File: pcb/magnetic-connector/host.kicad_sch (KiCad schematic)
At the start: 8 parts

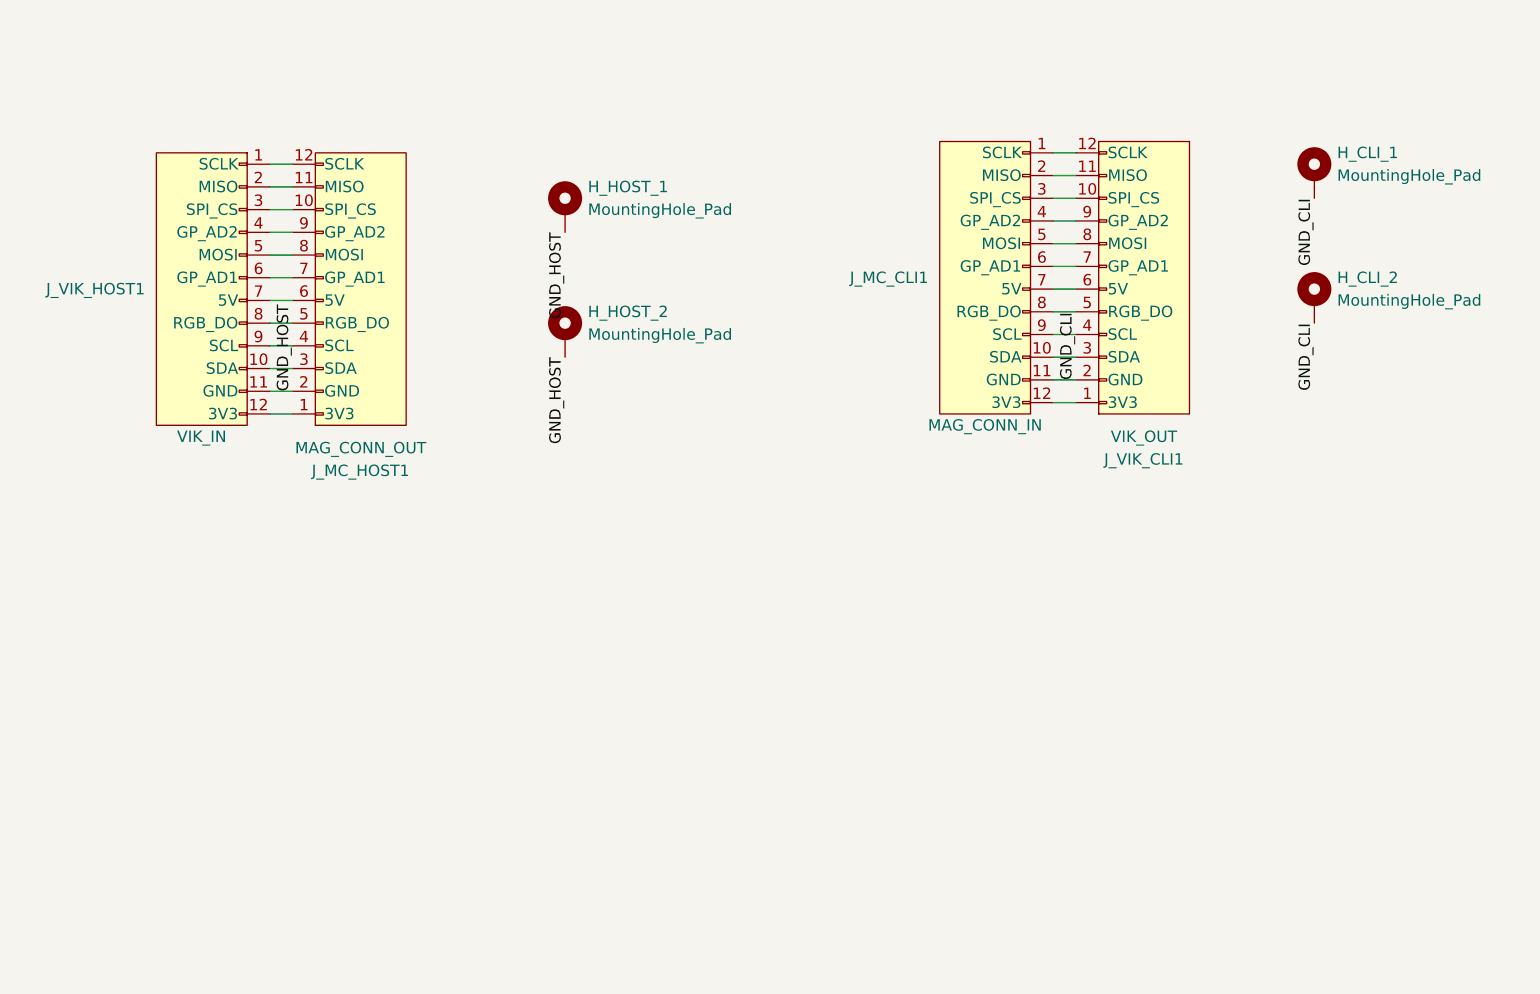
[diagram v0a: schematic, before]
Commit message: Make magnetic connector size compliant with VIK small form factor.
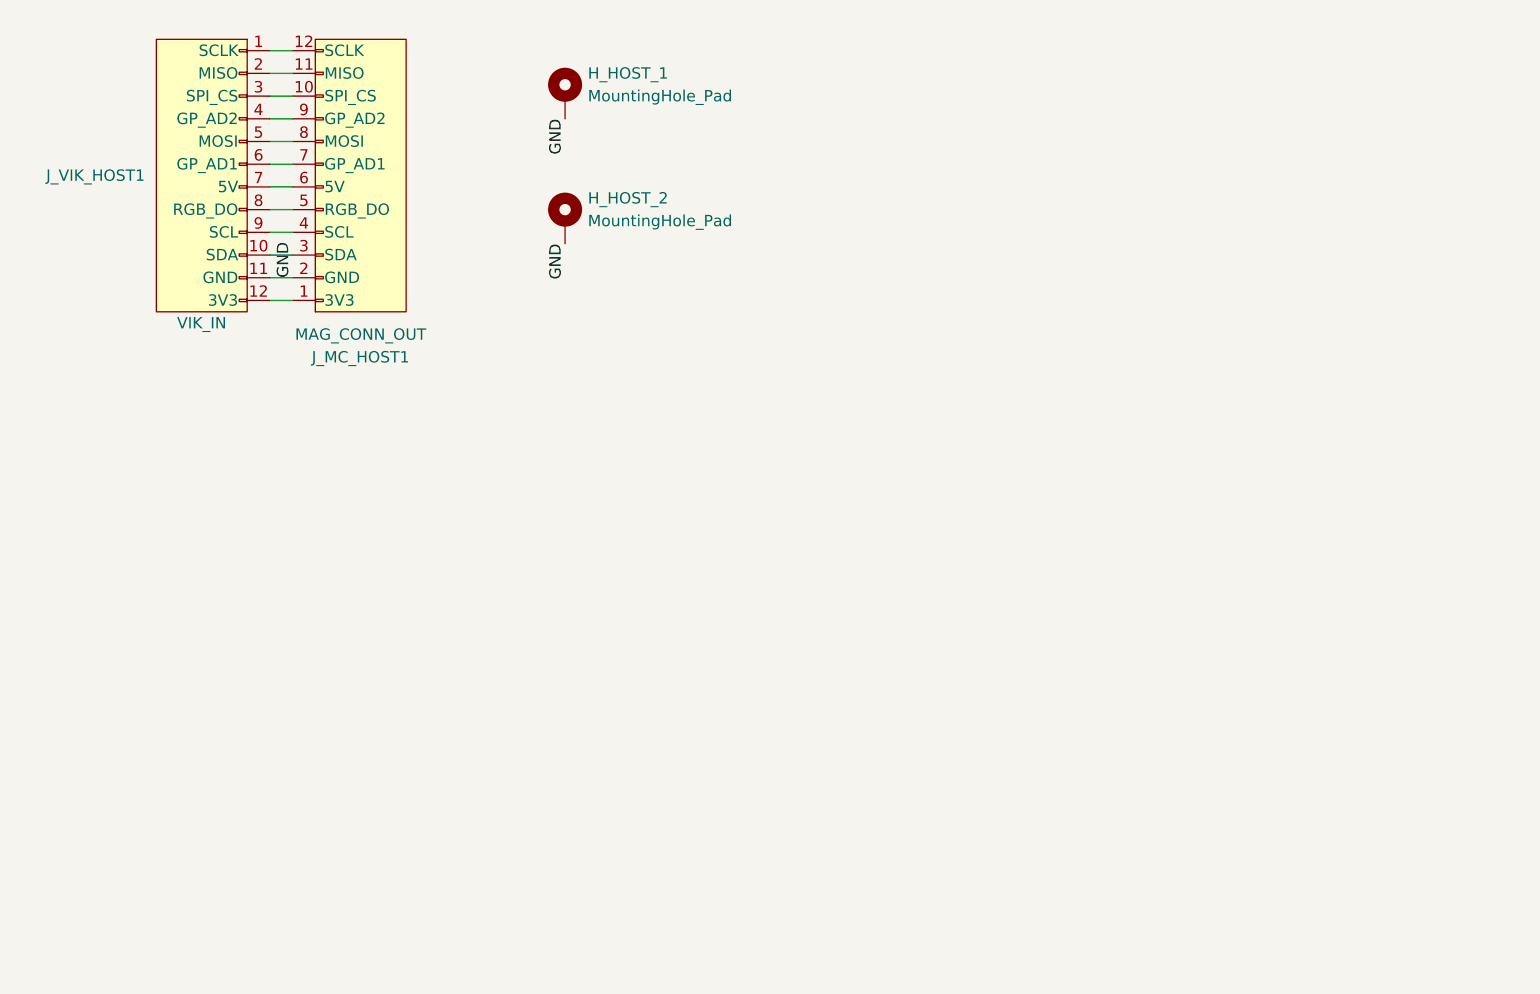
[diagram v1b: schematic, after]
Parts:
- removed H_CLI_1, H_CLI_2: MountingHole_Pad, MountingHole:MountingHole_2.2mm_M2_Pad, symbol Mechanical:MountingHole_Pad
- removed J_MC_CLI1: MAG_CONN_IN, magnetic-connector:vik-module-throughole-2.2mm, symbol vik:vik-module-connector
- removed J_VIK_CLI1: VIK_OUT, vik:vik-keyboard-connector-vertical, symbol vik:vik-keyboard-connector
- H_HOST_1, H_HOST_2: footprint MountingHole:MountingHole_2.2mm_M2_Pad -> MountingHole:MountingHole_2.2mm_M2
- J_MC_HOST1: footprint magnetic-connector:vik-keyboard-throughole-2.2mm -> vik:vik-keyboard-throughole-2.2mm
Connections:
- net GND_HOST renamed GND

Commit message: Add ESD protection to magnetic connector module.
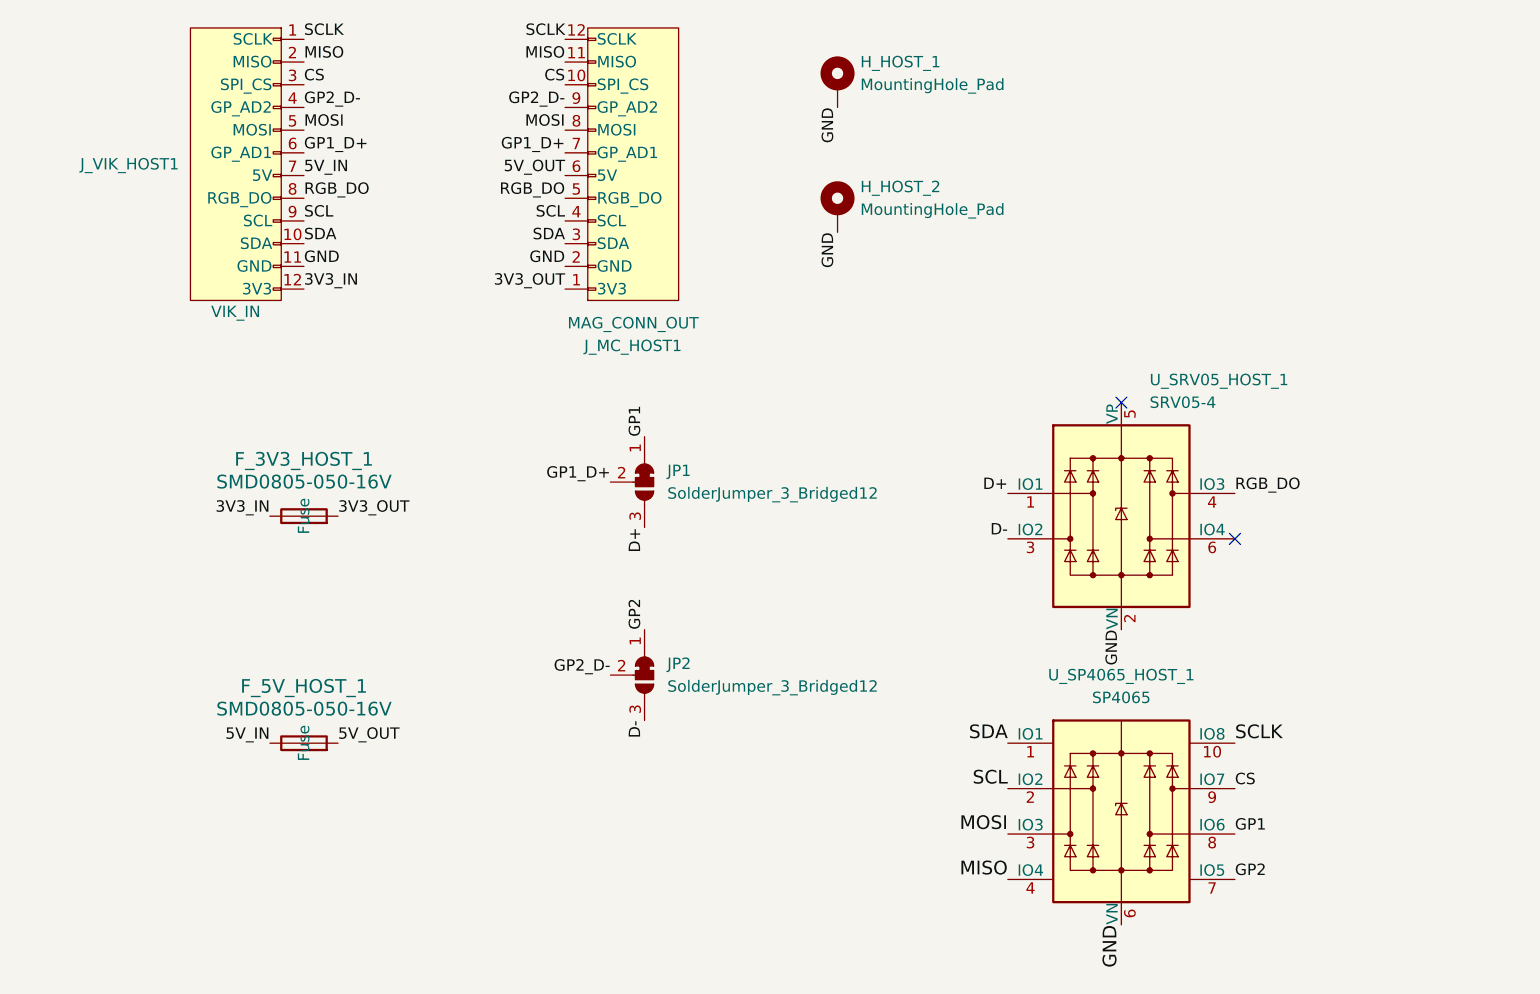
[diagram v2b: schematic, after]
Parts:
- added F_3V3_HOST_1, F_5V_HOST_1: SMD0805-050-16V, Fuse:Fuse_0805_2012Metric, symbol Device:Fuse
- added JP1, JP2: SolderJumper_3_Bridged12, Jumper:SolderJumper-3_P1.3mm_Bridged12_RoundedPad1.0x1.5mm_NumberLabels, symbol Jumper:SolderJumper_3_Bridged12
- added U_SP4065_HOST_1: SP4065, Package_SO:MSOP-10-1EP_3x3mm_P0.5mm_EP1.68x1.88mm, symbol SP4065:SP4065
- added U_SRV05_HOST_1: SRV05-4, Package_TO_SOT_SMD:SOT-23-6, symbol Power_Protection:SRV05-4
- H_HOST_1, H_HOST_2: footprint MountingHole:MountingHole_2.2mm_M2 -> MountingHole:MountingHole_2.2mm_M2_Pad
- J_MC_HOST1: footprint vik:vik-keyboard-throughole-2.2mm -> magnetic-connector:vik-keyboard-throughole-2.2mm
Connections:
- net GND: now also U_SP4065_HOST_1.6 (VN), U_SRV05_HOST_1.2 (VN)
- net SCLK: now reaches J_MC_HOST1.12 (SCLK), J_VIK_HOST1.1 (SCLK)
- net SCLK: now also U_SP4065_HOST_1.10 (IO8)
- net SDA: now reaches J_MC_HOST1.3 (SDA), J_VIK_HOST1.10 (SDA)
- net SDA: now also U_SP4065_HOST_1.1 (IO1)
- net 3V3_IN: now reaches J_VIK_HOST1.12 (3V3)
- net 3V3_IN: now also F_3V3_HOST_1.1; no longer J_MC_HOST1.1 (3V3)
- net MISO: now reaches J_MC_HOST1.11 (MISO), J_VIK_HOST1.2 (MISO)
- net MISO: now also U_SP4065_HOST_1.4 (IO4)
- net CS: now reaches J_MC_HOST1.10 (SPI_CS), J_VIK_HOST1.3 (SPI_CS)
- net CS: now also U_SP4065_HOST_1.9 (IO7)
- net GP2_D-: now reaches J_MC_HOST1.9 (GP_AD2), J_VIK_HOST1.4 (GP_AD2)
- net GP2_D-: now also JP2.2 (C)
- net MOSI: now reaches J_MC_HOST1.8 (MOSI), J_VIK_HOST1.5 (MOSI)
- net MOSI: now also U_SP4065_HOST_1.3 (IO3)
- net GP1_D+: now reaches J_MC_HOST1.7 (GP_AD1), J_VIK_HOST1.6 (GP_AD1)
- net GP1_D+: now also JP1.2 (C)
- net 5V_IN: now reaches J_VIK_HOST1.7 (5V)
- net 5V_IN: now also F_5V_HOST_1.1; no longer J_MC_HOST1.6 (5V)
- net RGB_DO: now reaches J_MC_HOST1.5 (RGB_DO), J_VIK_HOST1.8 (RGB_DO)
- net RGB_DO: now also U_SRV05_HOST_1.4 (IO3)
- net SCL: now reaches J_MC_HOST1.4 (SCL), J_VIK_HOST1.9 (SCL)
- net SCL: now also U_SP4065_HOST_1.2 (IO2)
- new net 3V3_OUT: F_3V3_HOST_1.2, J_MC_HOST1.1 (3V3)
- new net 5V_OUT: F_5V_HOST_1.2, J_MC_HOST1.6 (5V)
- new net D+: JP1.3 (B), U_SRV05_HOST_1.1 (IO1)
- new net D-: JP2.3 (B), U_SRV05_HOST_1.3 (IO2)
- new net GP1: JP1.1 (A), U_SP4065_HOST_1.8 (IO6)
- new net GP2: JP2.1 (A), U_SP4065_HOST_1.7 (IO5)
- no-connect marks 0 -> 2

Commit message: Change VIK connector and ESD protection chips.
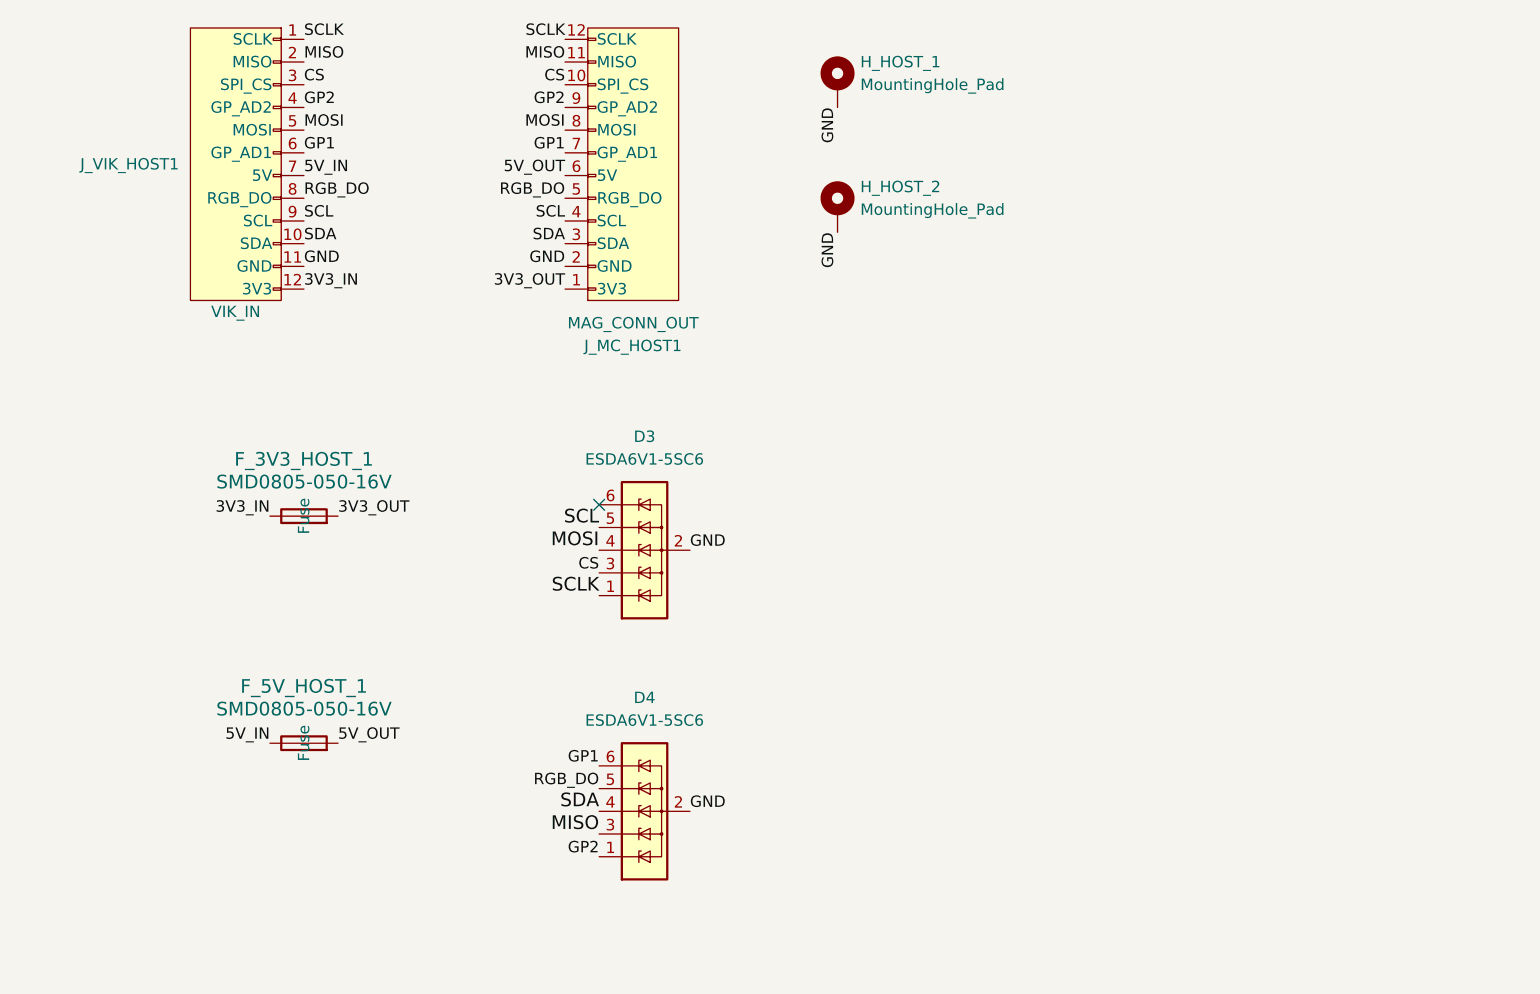
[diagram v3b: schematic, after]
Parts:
- removed JP1, JP2: SolderJumper_3_Bridged12, Jumper:SolderJumper-3_P1.3mm_Bridged12_RoundedPad1.0x1.5mm_NumberLabels, symbol Jumper:SolderJumper_3_Bridged12
- removed U_SP4065_HOST_1: SP4065, Package_SO:MSOP-10-1EP_3x3mm_P0.5mm_EP1.68x1.88mm, symbol SP4065:SP4065
- removed U_SRV05_HOST_1: SRV05-4, Package_TO_SOT_SMD:SOT-23-6, symbol Power_Protection:SRV05-4
- added D3, D4: ESDA6V1-5SC6, Package_TO_SOT_SMD:SOT-23-6, symbol Power_Protection:ESDA6V1-5SC6
- J_VIK_HOST1: footprint vik:vik-module-connector-vertical -> vik:vik-module-connector-horizontal
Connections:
- net GP1_D+ is gone; now on net GP1: J_MC_HOST1.7 (GP_AD1), J_VIK_HOST1.6 (GP_AD1)
- net GP2_D- is gone; now on net GP2: J_MC_HOST1.9 (GP_AD2), J_VIK_HOST1.4 (GP_AD2)
- net CS: now also D3.3 (IO2)
- net GND: now also D3.2 (GND), D4.2 (GND)
- net GP1: now also D4.6 (IO5)
- net GP2: now also D4.1 (IO1)
- net MISO: now also D4.3 (IO2)
- net MOSI: now also D3.4 (IO3)
- net RGB_DO: now also D4.5 (IO4)
- net SCL: now also D3.5 (IO4)
- net SCLK: now also D3.1 (IO1)
- net SDA: now also D4.4 (IO3)
- no-connect marks 2 -> 1
